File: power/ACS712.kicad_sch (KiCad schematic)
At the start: 3 parts, among them U5 ACS712xLCTR-30A

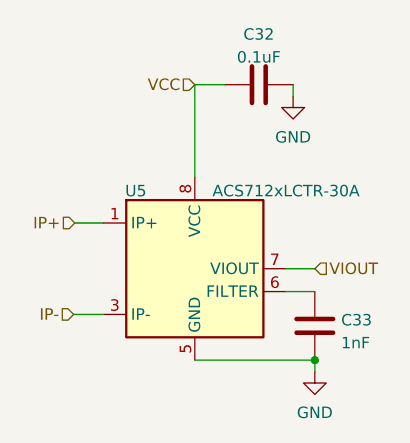
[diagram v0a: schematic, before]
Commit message: Feat: Completed footprint assignment, began part placement
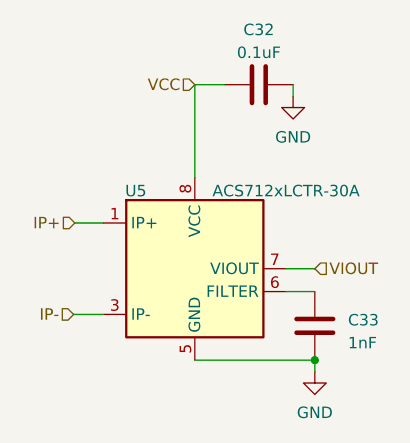
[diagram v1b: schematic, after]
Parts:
- C32, C33: footprint (none) -> Capacitor_SMD:C_0603_1608Metric
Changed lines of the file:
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@@
   (symbol (lib_id "Device:C") (at 157.734 84.836 90) (unit 1)
     (in_bom yes) (on_board yes) (dnp no) (fields_autoplaced)
-    (property "Reference" "C32" (at 157.734 79.248 90)
+    (property "Reference" "C32" (at 157.734 78.74 90)
       (effects (font (size 1.27 1.27)))
     )
-    (property "Value" "0.1uF" (at 157.734 81.788 90)
+    (property "Value" "0.1uF" (at 157.734 81.28 90)
       (effects (font (size 1.27 1.27)))
     )
-    (property "Footprint" "" (at 161.544 83.8708 0)
+    (property "Footprint" "Capacitor_SMD:C_0603_1608Metric" (at 161.544 83.8708 0)
       (effects (font (size 1.27 1.27)) hide)
     )
@@
         )
         (path "/6d3c5c52-febb-4c99-82d7-f9b22bb5762b/67d6e32f-48e8-4582-a115-95fda843ec4d"
-          (reference "C32") (unit 1)
+          (reference "C31") (unit 1)
         )
       )
@@
   (symbol (lib_id "Device:C") (at 163.957 111.633 0) (unit 1)
     (in_bom yes) (on_board yes) (dnp no) (fields_autoplaced)
-    (property "Reference" "C33" (at 166.878 110.998 0)
+    (property "Reference" "C33" (at 167.64 110.998 0)
       (effects (font (size 1.27 1.27)) (justify left))
     )
-    (property "Value" "1nF" (at 166.878 113.538 0)
+    (property "Value" "1nF" (at 167.64 113.538 0)
       (effects (font (size 1.27 1.27)) (justify left))
     )
-    (property "Footprint" "" (at 164.9222 115.443 0)
+    (property "Footprint" "Capacitor_SMD:C_0603_1608Metric" (at 164.9222 115.443 0)
       (effects (font (size 1.27 1.27)) hide)
     )
@@
         )
         (path "/6d3c5c52-febb-4c99-82d7-f9b22bb5762b/67d6e32f-48e8-4582-a115-95fda843ec4d"
-          (reference "C33") (unit 1)
+          (reference "C32") (unit 1)
         )
       )
